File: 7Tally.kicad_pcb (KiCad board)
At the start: 2 copper layers, 56 x 38 mm, 50 parts, among them J2 B2B-PH-K-S_LF__SN_, P1 53047-0310, SW1 TL3300CF160Q, U1 ESP32-C3_SUPERMINI_TH, U2 BQ21040DBVR, U3 TC1263-3.3VOA

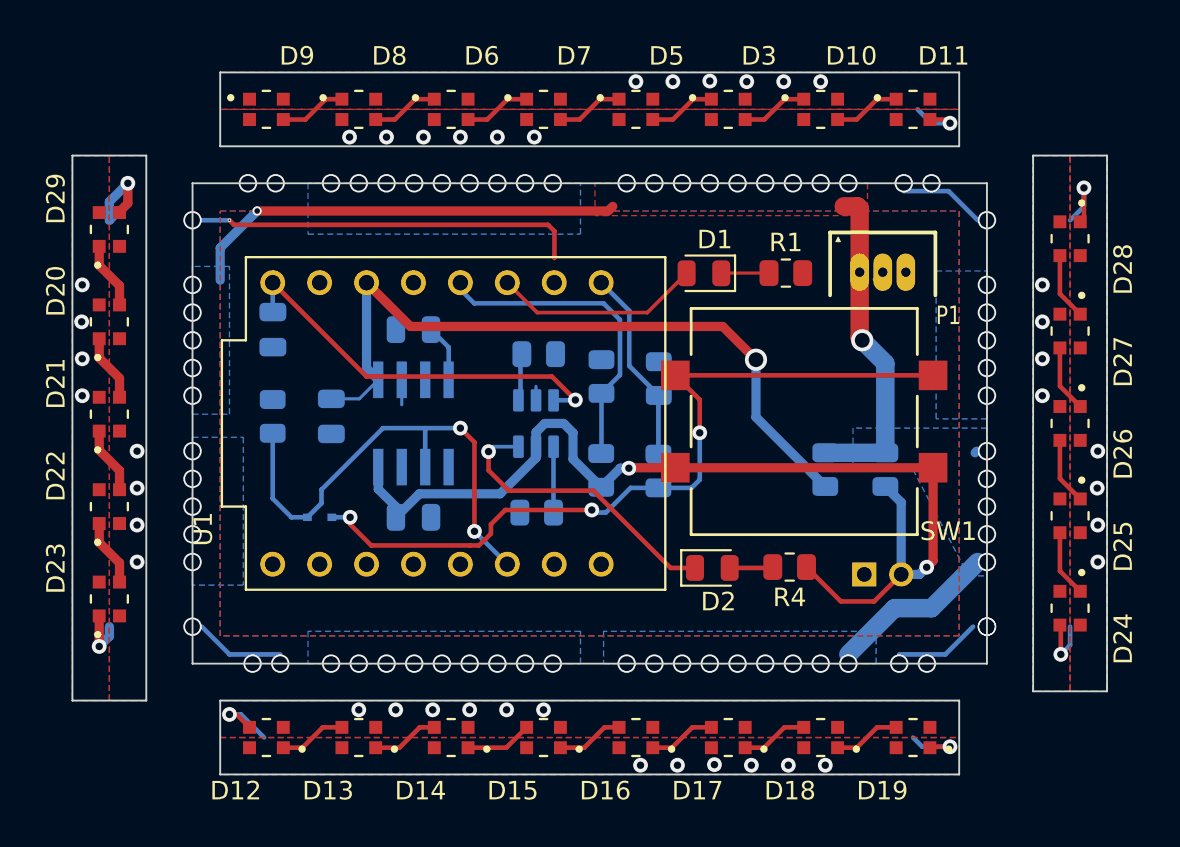
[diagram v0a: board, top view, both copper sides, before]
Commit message: feat(PCB): Panelization
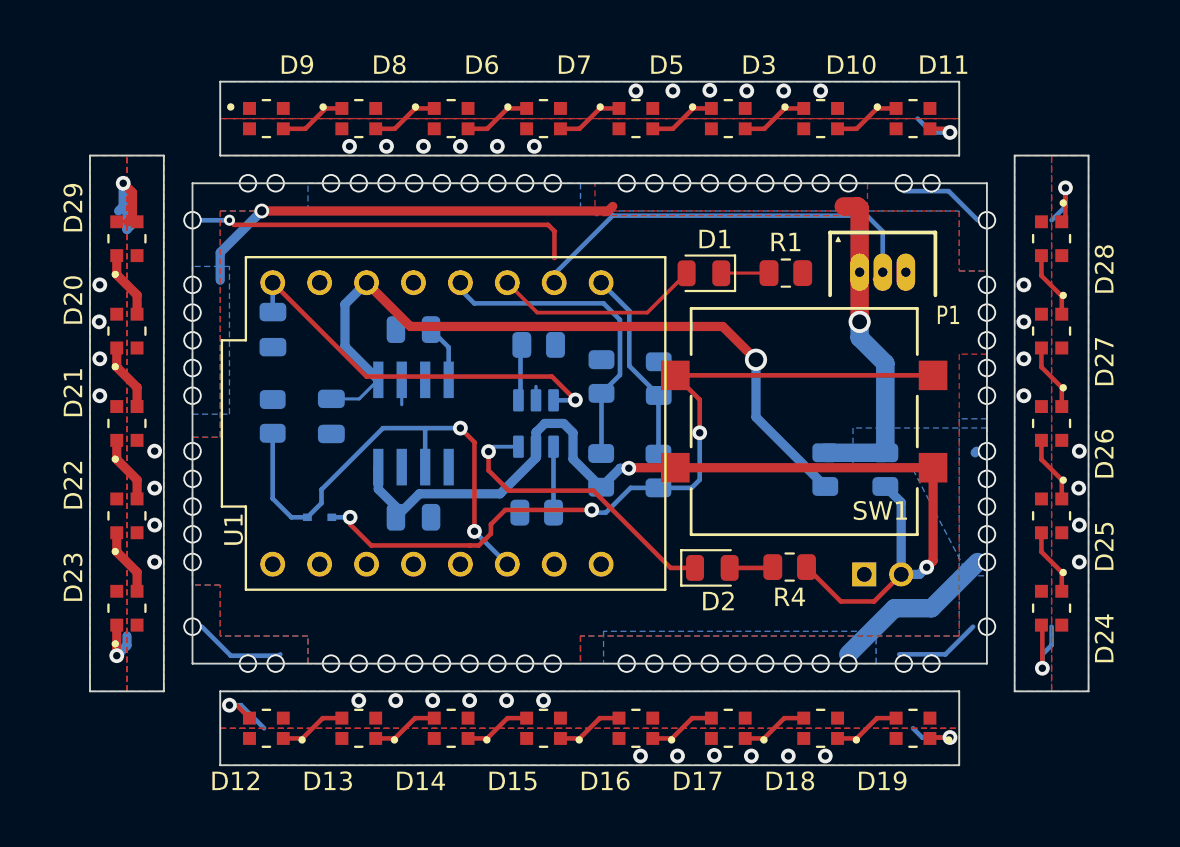
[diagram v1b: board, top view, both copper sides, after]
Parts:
- moved D20 1.07 mm to (45.5, 58.5)
- moved D21 1.07 mm to (45.5, 63.5)
- moved D22 1.07 mm to (45.5, 68.5)
- moved D23 1.07 mm to (45.5, 73.5)
- moved D29 1.07 mm to (45.5, 53.5)
- moved D24 1.00 mm to (95.5, 73.5)
- moved D25 1.00 mm to (95.5, 68.5)
- moved D26 1.00 mm to (95.5, 63.5)
- moved D27 1.00 mm to (95.5, 58.5)
- moved D28 1.00 mm to (95.5, 53.5)
- moved D10 0.50 mm to (83.0, 47.0)
- moved D11 0.50 mm to (88.0, 47.0)
- moved D12 0.50 mm to (53.0, 80.0)
- moved D13 0.50 mm to (58.0, 80.0)
- moved D14 0.50 mm to (63.0, 80.0)
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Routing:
- net NEOPIXEL_PIN: track 26.6 -> 49.5 mm
- net Net-(D19-DO): track 11.2 -> 12.7 mm, vias 6 -> 5
- net +3.3V: track 40.1 -> 41.1 mm
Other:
- board size 56 x 38 mm -> 54 x 37 mm
